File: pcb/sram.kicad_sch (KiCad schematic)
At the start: 2 parts

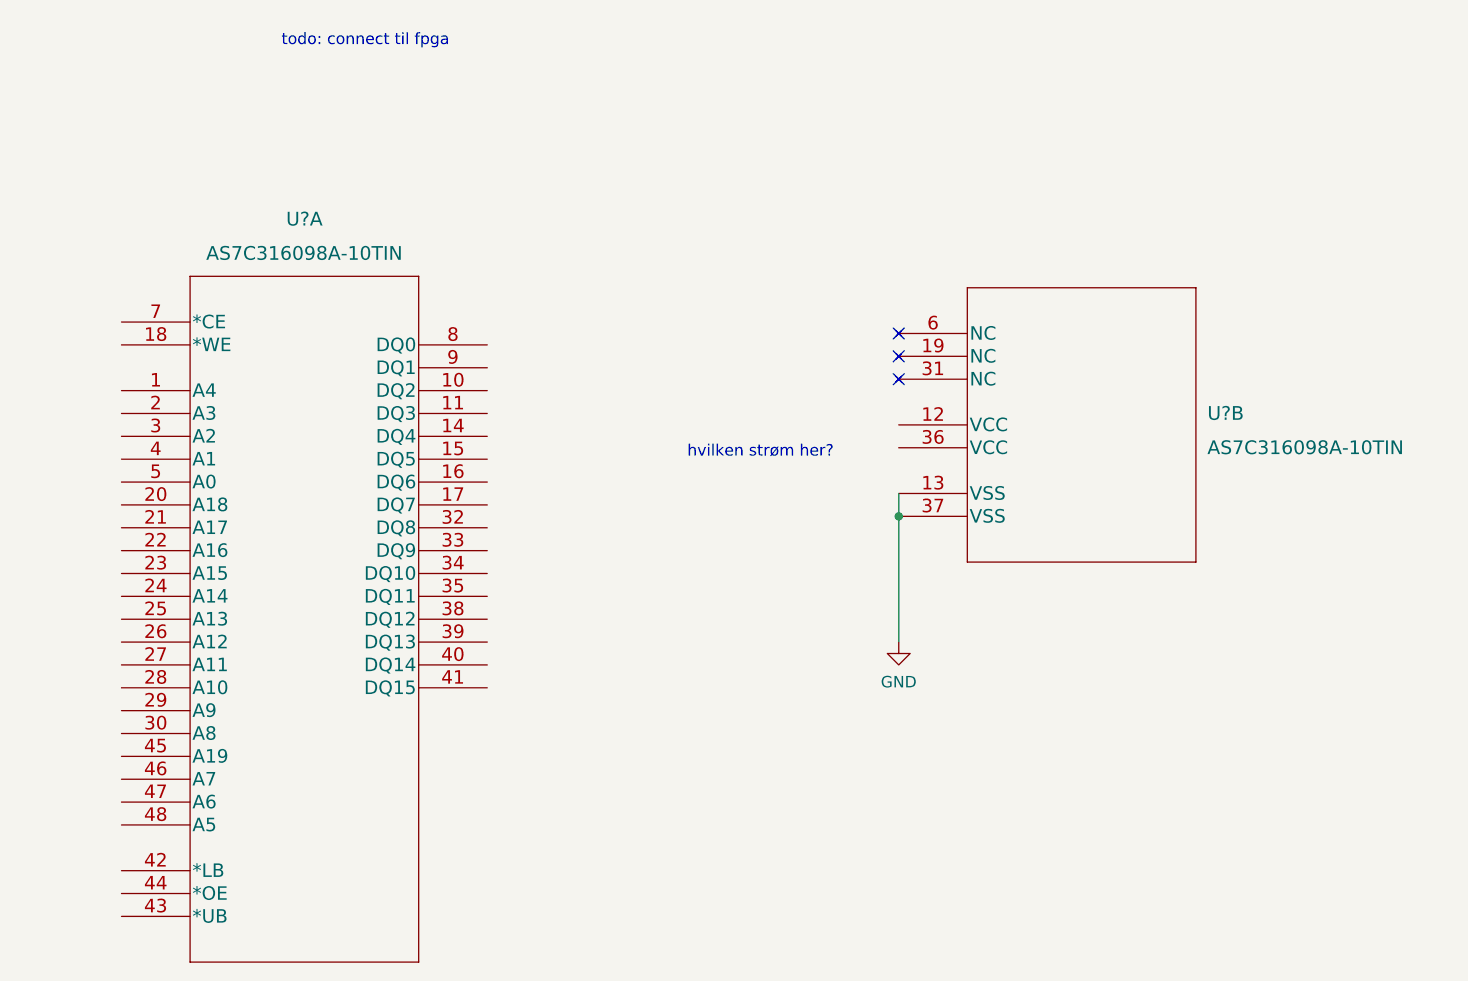
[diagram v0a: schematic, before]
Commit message: connect sram and vga to fpga
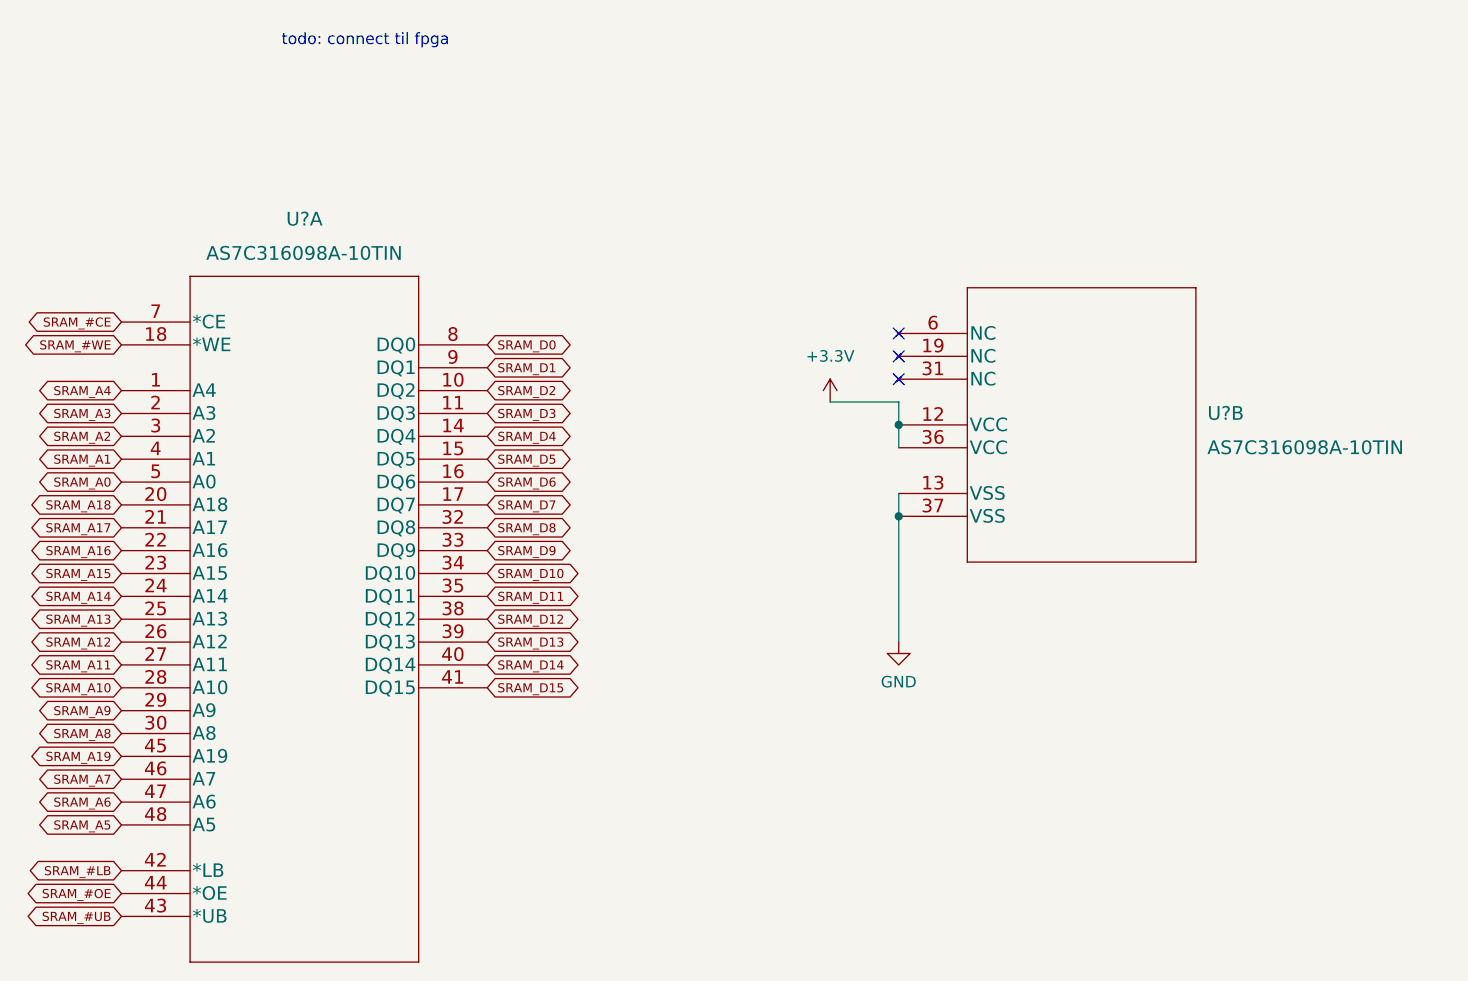
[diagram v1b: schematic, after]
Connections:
- net +3.3V: now reaches U?.12 (VCC)
- net +3.3V: now also U?.36 (VCC)
- net SRAM_A4: now reaches U?.1 (A4)
- net SRAM_D2: now reaches U?.10 (DQ2)
- net SRAM_D3: now reaches U?.11 (DQ3)
- net SRAM_D4: now reaches U?.14 (DQ4)
- net SRAM_D5: now reaches U?.15 (DQ5)
- net SRAM_D6: now reaches U?.16 (DQ6)
- net SRAM_D7: now reaches U?.17 (DQ7)
- net SRAM_#WE: now reaches U?.18 (*WE)
- net SRAM_A3: now reaches U?.2 (A3)
- net SRAM_A18: now reaches U?.20 (A18)
- net SRAM_A17: now reaches U?.21 (A17)
- net SRAM_A16: now reaches U?.22 (A16)
- net SRAM_A15: now reaches U?.23 (A15)
- net SRAM_A14: now reaches U?.24 (A14)
- net SRAM_A13: now reaches U?.25 (A13)
- net SRAM_A12: now reaches U?.26 (A12)
- net SRAM_A11: now reaches U?.27 (A11)
- net SRAM_A10: now reaches U?.28 (A10)
- net SRAM_A9: now reaches U?.29 (A9)
- net SRAM_A2: now reaches U?.3 (A2)
- net SRAM_A8: now reaches U?.30 (A8)
- net SRAM_D8: now reaches U?.32 (DQ8)
- net SRAM_D9: now reaches U?.33 (DQ9)
- net SRAM_D10: now reaches U?.34 (DQ10)
- net SRAM_D11: now reaches U?.35 (DQ11)
- net SRAM_D12: now reaches U?.38 (DQ12)
- net SRAM_D13: now reaches U?.39 (DQ13)
- net SRAM_A1: now reaches U?.4 (A1)
- net SRAM_D14: now reaches U?.40 (DQ14)
- net SRAM_D15: now reaches U?.41 (DQ15)
- net SRAM_#LB: now reaches U?.42 (*LB)
- net SRAM_#UB: now reaches U?.43 (*UB)
- net SRAM_#OE: now reaches U?.44 (*OE)
- net SRAM_A19: now reaches U?.45 (A19)
- net SRAM_A7: now reaches U?.46 (A7)
- net SRAM_A6: now reaches U?.47 (A6)
- net SRAM_A5: now reaches U?.48 (A5)
- net SRAM_A0: now reaches U?.5 (A0)
- net SRAM_#CE: now reaches U?.7 (*CE)
- net SRAM_D0: now reaches U?.8 (DQ0)
- net SRAM_D1: now reaches U?.9 (DQ1)
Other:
- note removed: "hvilken strøm her?"

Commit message: maybe finished schematic
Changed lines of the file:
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@@
   (no_connect (at 119.38 78.74))
   (no_connect (at 119.38 81.28))
-  (wire (pts (xy 119.38 83.82) (xy 111.76 83.82))
+  (wire (pts (xy 119.38 86.36) (xy 113.03 86.36))
     (stroke (width 0) (type default) (color 0 0 0 0))
   )
@@
     (stroke (width 0) (type default) (color 0 0 0 0))
   )
-  (wire (pts (xy 119.38 86.36) (xy 119.38 83.82))
-    (stroke (width 0) (type default) (color 0 0 0 0))
-  )
-  (wire (pts (xy 119.38 96.52) (xy 119.38 110.49))
+  (wire (pts (xy 119.38 96.52) (xy 119.38 100.33))
     (stroke (width 0) (type default) (color 0 0 0 0))
   )
@@
     (pin "6")
   )
-  (symbol (lib_id "power:+3.3V") (at 111.76 83.82 0) (unit 1)
+  (symbol (lib_id "power:+3.3V") (at 113.03 86.36 0) (unit 1)
     (in_bom yes) (on_board yes) (fields_autoplaced)
-    (property "Reference" "#PWR?" (id 0) (at 111.76 87.63 0)
-      (effects (font (size 1.27 1.27)) hide)
-    )
-    (property "Value" "+3.3V" (id 1) (at 111.76 78.74 0))
-    (property "Footprint" "" (id 2) (at 111.76 83.82 0)
-      (effects (font (size 1.27 1.27)) hide)
-    )
-    (property "Datasheet" "" (id 3) (at 111.76 83.82 0)
+    (property "Reference" "#PWR?" (id 0) (at 113.03 90.17 0)
+      (effects (font (size 1.27 1.27)) hide)
+    )
+    (property "Value" "+3.3V" (id 1) (at 113.03 81.28 0))
+    (property "Footprint" "" (id 2) (at 113.03 86.36 0)
+      (effects (font (size 1.27 1.27)) hide)
+    )
+    (property "Datasheet" "" (id 3) (at 113.03 86.36 0)
       (effects (font (size 1.27 1.27)) hide)
     )
     (pin "1")
   )
-  (symbol (lib_id "power:GND") (at 119.38 110.49 0) (unit 1)
+  (symbol (lib_id "power:GND") (at 119.38 100.33 0) (unit 1)
     (in_bom yes) (on_board yes) (fields_autoplaced)
-    (property "Reference" "#PWR?" (id 0) (at 119.38 116.84 0)
-      (effects (font (size 1.27 1.27)) hide)
-    )
-    (property "Value" "GND" (id 1) (at 119.38 114.935 0))
-    (property "Footprint" "" (id 2) (at 119.38 110.49 0)
-      (effects (font (size 1.27 1.27)) hide)
-    )
-    (property "Datasheet" "" (id 3) (at 119.38 110.49 0)
-      (effects (font (size 1.27 1.27)) hide)
-    )
+    (property "Reference" "#PWR?" (id 0) (at 119.38 106.68 0)
+      (effects (font (size 1.27 1.27)) hide)
+    )
+    (property "Value" "GND" (id 1) (at 119.38 104.775 0))
+    (property "Footprint" "" (id 2) (at 119.38 100.33 0)
+      (effects (font (size 1.27 1.27)) hide)
+    )
+    (property "Datasheet" "" (id 3) (at 119.38 100.33 0)
+      (effects (font (size 1.27 1.27)) hide)
+    )

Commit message: everything except crystal
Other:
- note removed: "todo: connect til fpga"
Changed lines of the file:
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@@
   (junction (at 119.38 86.36) (diameter 0) (color 0 0 0 0)
   )
-  (junction (at 119.38 96.52) (diameter 0) (color 0 0 0 0)
+  (junction (at 119.38 93.98) (diameter 0) (color 0 0 0 0)
   )
   (no_connect (at 119.38 76.2))
   (no_connect (at 119.38 78.74))
   (no_connect (at 119.38 81.28))
-  (wire (pts (xy 119.38 86.36) (xy 113.03 86.36))
-    (stroke (width 0) (type default) (color 0 0 0 0))
-  )
   (wire (pts (xy 119.38 93.98) (xy 119.38 96.52))
     (stroke (width 0) (type default) (color 0 0 0 0))
   )
-  (wire (pts (xy 119.38 96.52) (xy 119.38 100.33))
-    (stroke (width 0) (type default) (color 0 0 0 0))
-  )
   (wire (pts (xy 119.38 88.9) (xy 119.38 86.36))
     (stroke (width 0) (type default) (color 0 0 0 0))
-  )
-  (text "todo: connect til fpga" (at 50.8 44.45 0)
-    (effects (font (size 1.27 1.27)) (justify left bottom))
   )
   (global_label "SRAM_D5" (shape bidirectional) (at 73.66 90.17 0) (fields_autoplaced)
@@
     (pin "6")
   )
-  (symbol (lib_id "power:+3.3V") (at 113.03 86.36 0) (unit 1)
+  (symbol (lib_id "power:+3.3V") (at 119.38 86.36 90) (unit 1)
     (in_bom yes) (on_board yes) (fields_autoplaced)
-    (property "Reference" "#PWR?" (id 0) (at 113.03 90.17 0)
-      (effects (font (size 1.27 1.27)) hide)
-    )
-    (property "Value" "+3.3V" (id 1) (at 113.03 81.28 0))
-    (property "Footprint" "" (id 2) (at 113.03 86.36 0)
-      (effects (font (size 1.27 1.27)) hide)
-    )
-    (property "Datasheet" "" (id 3) (at 113.03 86.36 0)
+    (property "Reference" "#PWR?" (id 0) (at 123.19 86.36 0)
+      (effects (font (size 1.27 1.27)) hide)
+    )
+    (property "Value" "+3.3V" (id 1) (at 115.57 86.3599 90)
+      (effects (font (size 1.27 1.27)) (justify left))
+    )
+    (property "Footprint" "" (id 2) (at 119.38 86.36 0)
+      (effects (font (size 1.27 1.27)) hide)
+    )
+    (property "Datasheet" "" (id 3) (at 119.38 86.36 0)
       (effects (font (size 1.27 1.27)) hide)
     )
     (pin "1")
   )
-  (symbol (lib_id "power:GND") (at 119.38 100.33 0) (unit 1)
+  (symbol (lib_id "power:GND") (at 119.38 93.98 270) (unit 1)
     (in_bom yes) (on_board yes) (fields_autoplaced)
-    (property "Reference" "#PWR?" (id 0) (at 119.38 106.68 0)
-      (effects (font (size 1.27 1.27)) hide)
-    )
-    (property "Value" "GND" (id 1) (at 119.38 104.775 0))
-    (property "Footprint" "" (id 2) (at 119.38 100.33 0)
-      (effects (font (size 1.27 1.27)) hide)
-    )
-    (property "Datasheet" "" (id 3) (at 119.38 100.33 0)
-      (effects (font (size 1.27 1.27)) hide)
-    )
+    (property "Reference" "#PWR?" (id 0) (at 113.03 93.98 0)
+      (effects (font (size 1.27 1.27)) hide)
+    )
+    (property "Value" "GND" (id 1) (at 115.57 93.9799 90)
+      (effects (font (size 1.27 1.27)) (justify right))
+    )
+    (property "Footprint" "" (id 2) (at 119.38 93.98 0)
+      (effects (font (size 1.27 1.27)) hide)
+    )
+    (property "Datasheet" "" (id 3) (at 119.38 93.98 0)
+      (effects (font (size 1.27 1.27)) hide)
+    )

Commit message: add oscilattor + spi debug+ cap on sramd
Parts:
- added C? (x2): 100n, symbol Device:C
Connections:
- net +3.3V: now also C?.2, C?.2
- net GND: now also C?.1, C?.1
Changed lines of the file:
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@@
 (kicad_sch (version 20211123) (generator eeschema)
   (paper "A4")
-  (junction (at 119.38 86.36) (diameter 0) (color 0 0 0 0)
-  )
-  (junction (at 119.38 93.98) (diameter 0) (color 0 0 0 0)
+  (junction (at 111.76 86.36) (diameter 0) (color 0 0 0 0)
+  )
+  (junction (at 101.6 63.5) (diameter 0) (color 0 0 0 0)
+  )
+  (junction (at 87.63 55.88) (diameter 0) (color 0 0 0 0)
+  )
+  (junction (at 119.38 96.52) (diameter 0) (color 0 0 0 0)
   )
   (no_connect (at 119.38 76.2))
   (no_connect (at 119.38 78.74))
   (no_connect (at 119.38 81.28))
+  (wire (pts (xy 87.63 52.07) (xy 87.63 55.88))
+    (stroke (width 0) (type default) (color 0 0 0 0))
+  )
+  (wire (pts (xy 111.76 86.36) (xy 111.76 85.09))
+    (stroke (width 0) (type default) (color 0 0 0 0))
+  )
+  (wire (pts (xy 119.38 88.9) (xy 111.76 88.9))
+    (stroke (width 0) (type default) (color 0 0 0 0))
+  )
+  (wire (pts (xy 87.63 55.88) (xy 101.6 55.88))
+    (stroke (width 0) (type default) (color 0 0 0 0))
+  )
+  (wire (pts (xy 119.38 96.52) (xy 119.38 100.33))
+    (stroke (width 0) (type default) (color 0 0 0 0))
+  )
+  (wire (pts (xy 111.76 88.9) (xy 111.76 86.36))
+    (stroke (width 0) (type default) (color 0 0 0 0))
+  )
+  (wire (pts (xy 87.63 63.5) (xy 101.6 63.5))
+    (stroke (width 0) (type default) (color 0 0 0 0))
+  )
+  (wire (pts (xy 101.6 63.5) (xy 101.6 67.31))
+    (stroke (width 0) (type default) (color 0 0 0 0))
+  )
+  (wire (pts (xy 119.38 86.36) (xy 111.76 86.36))
+    (stroke (width 0) (type default) (color 0 0 0 0))
+  )
   (wire (pts (xy 119.38 93.98) (xy 119.38 96.52))
     (stroke (width 0) (type default) (color 0 0 0 0))
   )
-  (wire (pts (xy 119.38 88.9) (xy 119.38 86.36))
-    (stroke (width 0) (type default) (color 0 0 0 0))
-  )
   (global_label "SRAM_D5" (shape bidirectional) (at 73.66 90.17 0) (fields_autoplaced)
     (effects (font (size 1 1)) (justify left))
@@
       (effects (font (size 1 1)) (justify right) hide)
     )
+  )
+  (symbol (lib_id "power:+3.3V") (at 111.76 85.09 0) (unit 1)
+    (in_bom yes) (on_board yes) (fields_autoplaced)
+    (property "Reference" "#PWR?" (id 0) (at 111.76 88.9 0)
+      (effects (font (size 1.27 1.27)) hide)
+    )
+    (property "Value" "+3.3V" (id 1) (at 111.76 80.01 0))
+    (property "Footprint" "" (id 2) (at 111.76 85.09 0)
+      (effects (font (size 1.27 1.27)) hide)
+    )
+    (property "Datasheet" "" (id 3) (at 111.76 85.09 0)
+      (effects (font (size 1.27 1.27)) hide)
+    )
+    (pin "1")
+  )
+  (symbol (lib_id "Device:C") (at 101.6 59.69 180) (unit 1)
+    (in_bom yes) (on_board yes) (fields_autoplaced)
+    (property "Reference" "C?" (id 0) (at 105.41 58.4199 0)
+      (effects (font (size 1.27 1.27)) (justify right))
+    )
+    (property "Value" "100n" (id 1) (at 105.41 60.9599 0)
+      (effects (font (size 1.27 1.27)) (justify right))
+    )
+    (property "Footprint" "" (id 2) (at 100.6348 55.88 0)
+      (effects (font (size 1.27 1.27)) hide)
+    )
+    (property "Datasheet" "~" (id 3) (at 101.6 59.69 0)
+      (effects (font (size 1.27 1.27)) hide)
+    )
+    (pin "1")
+    (pin "2")
+  )
+  (symbol (lib_id "Device:C") (at 87.63 59.69 180) (unit 1)
+    (in_bom yes) (on_board yes) (fields_autoplaced)
+    (property "Reference" "C?" (id 0) (at 91.44 58.4199 0)
+      (effects (font (size 1.27 1.27)) (justify right))
+    )
+    (property "Value" "100n" (id 1) (at 91.44 60.9599 0)
+      (effects (font (size 1.27 1.27)) (justify right))
+    )
+    (property "Footprint" "" (id 2) (at 86.6648 55.88 0)
+      (effects (font (size 1.27 1.27)) hide)
+    )
+    (property "Datasheet" "~" (id 3) (at 87.63 59.69 0)
+      (effects (font (size 1.27 1.27)) hide)
+    )
+    (pin "1")
+    (pin "2")
   )
   (symbol (lib_id "sram:AS7C316098A-10TIN") (at 119.38 76.2 0) (unit 2)
@@
     (pin "6")
   )
-  (symbol (lib_id "power:+3.3V") (at 119.38 86.36 90) (unit 1)
-    (in_bom yes) (on_board yes) (fields_autoplaced)
-    (property "Reference" "#PWR?" (id 0) (at 123.19 86.36 0)
-      (effects (font (size 1.27 1.27)) hide)
-    )
-    (property "Value" "+3.3V" (id 1) (at 115.57 86.3599 90)
+  (symbol (lib_id "power:+3.3V") (at 87.63 52.07 0) (unit 1)
+    (in_bom yes) (on_board yes)
+    (property "Reference" "#PWR?" (id 0) (at 87.63 55.88 0)
+      (effects (font (size 1.27 1.27)) hide)
+    )
+    (property "Value" "+3.3V" (id 1) (at 87.63 48.26 90)
       (effects (font (size 1.27 1.27)) (justify left))
     )
-    (property "Footprint" "" (id 2) (at 119.38 86.36 0)
-      (effects (font (size 1.27 1.27)) hide)
-    )
-    (property "Datasheet" "" (id 3) (at 119.38 86.36 0)
-      (effects (font (size 1.27 1.27)) hide)
-    )
-    (pin "1")
-  )
-  (symbol (lib_id "power:GND") (at 119.38 93.98 270) (unit 1)
-    (in_bom yes) (on_board yes) (fields_autoplaced)
-    (property "Reference" "#PWR?" (id 0) (at 113.03 93.98 0)
-      (effects (font (size 1.27 1.27)) hide)
-    )
-    (property "Value" "GND" (id 1) (at 115.57 93.9799 90)
-      (effects (font (size 1.27 1.27)) (justify right))
-    )
-    (property "Footprint" "" (id 2) (at 119.38 93.98 0)
-      (effects (font (size 1.27 1.27)) hide)
-    )
-    (property "Datasheet" "" (id 3) (at 119.38 93.98 0)
-      (effects (font (size 1.27 1.27)) hide)
-    )
+    (property "Footprint" "" (id 2) (at 87.63 52.07 0)
+      (effects (font (size 1.27 1.27)) hide)
+    )
+    (property "Datasheet" "" (id 3) (at 87.63 52.07 0)
+      (effects (font (size 1.27 1.27)) hide)
+    )
+    (pin "1")
+  )
+  (symbol (lib_id "power:GND") (at 101.6 67.31 0) (unit 1)
+    (in_bom yes) (on_board yes) (fields_autoplaced)
+    (property "Reference" "#PWR?" (id 0) (at 101.6 73.66 0)
+      (effects (font (size 1.27 1.27)) hide)
+    )
+    (property "Value" "GND" (id 1) (at 101.6 72.39 0))
+    (property "Footprint" "" (id 2) (at 101.6 67.31 0)
+      (effects (font (size 1.27 1.27)) hide)
+    )
+    (property "Datasheet" "" (id 3) (at 101.6 67.31 0)
+      (effects (font (size 1.27 1.27)) hide)
+    )
+    (pin "1")
+  )
+  (symbol (lib_id "power:GND") (at 119.38 100.33 0) (unit 1)
+    (in_bom yes) (on_board yes) (fields_autoplaced)
+    (property "Reference" "#PWR?" (id 0) (at 119.38 106.68 0)
+      (effects (font (size 1.27 1.27)) hide)
+    )
+    (property "Value" "GND" (id 1) (at 119.38 105.41 0))
+    (property "Footprint" "" (id 2) (at 119.38 100.33 0)
+      (effects (font (size 1.27 1.27)) hide)
+    )
+    (property "Datasheet" "" (id 3) (at 119.38 100.33 0)
+      (effects (font (size 1.27 1.27)) hide)
+    )
